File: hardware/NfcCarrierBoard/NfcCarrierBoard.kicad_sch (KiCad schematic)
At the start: 50 parts, among them J1 Barrel_Jack, J2 Conn_01x03, J3 JST SH 4, J4 Grove, J5 Conn_01x03, J6 UART, J7 Grove UART, Q1 NMOS, Q2 NMOS, SW1 RESET, U1 24AA02E-OT

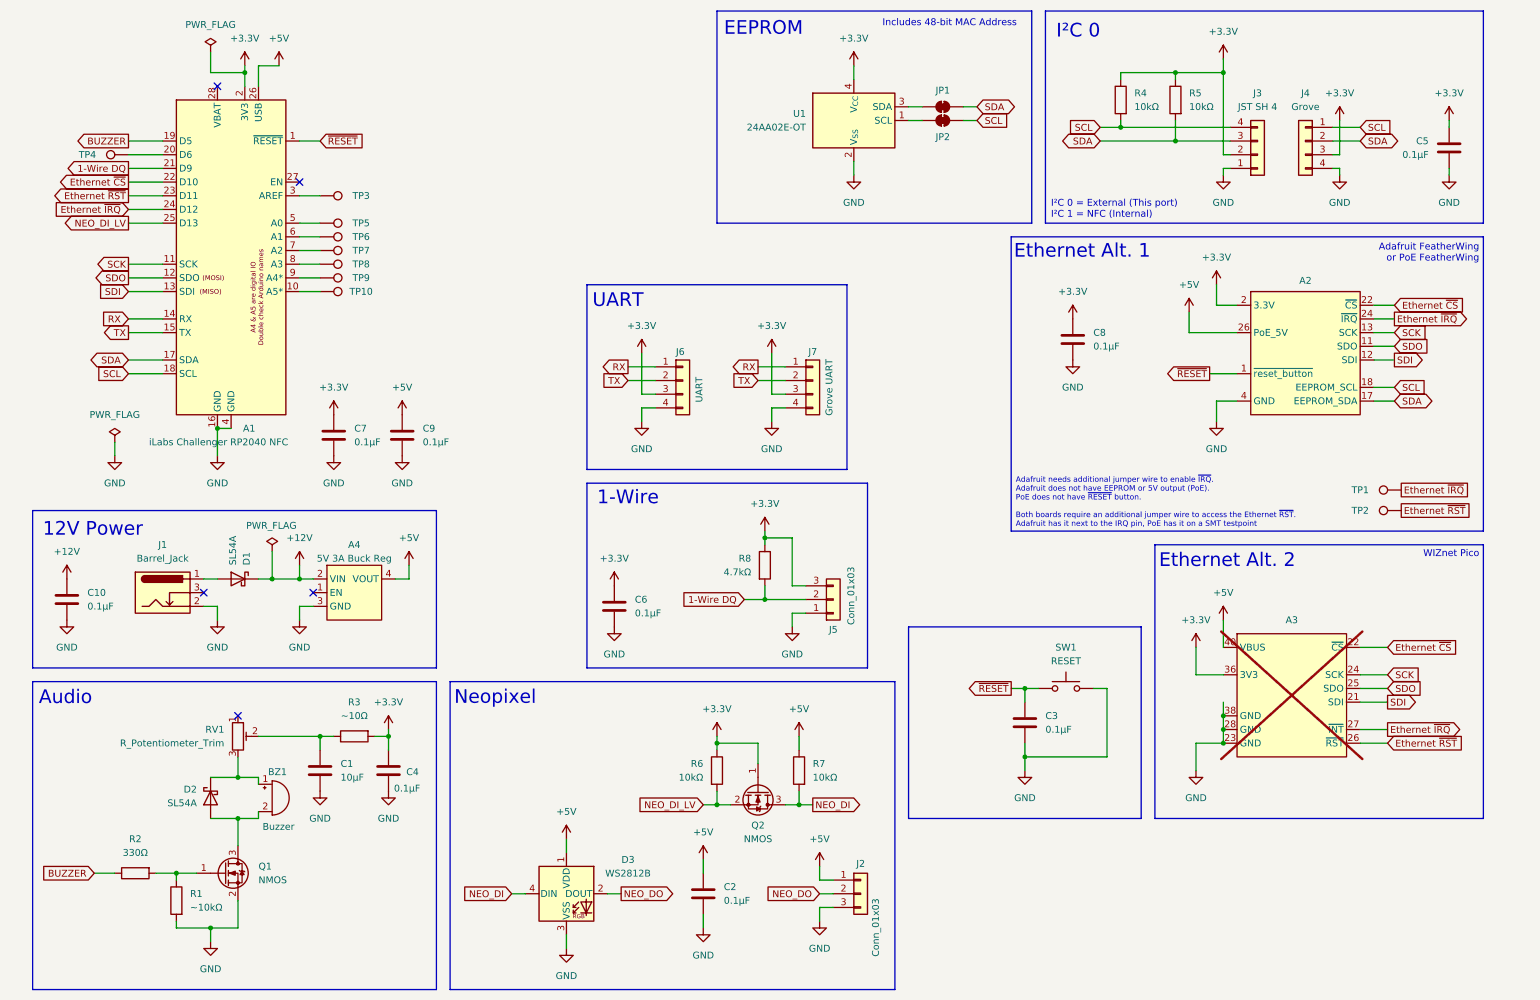
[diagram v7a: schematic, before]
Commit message: Add jumper to select between 3.3V and 5V for audio
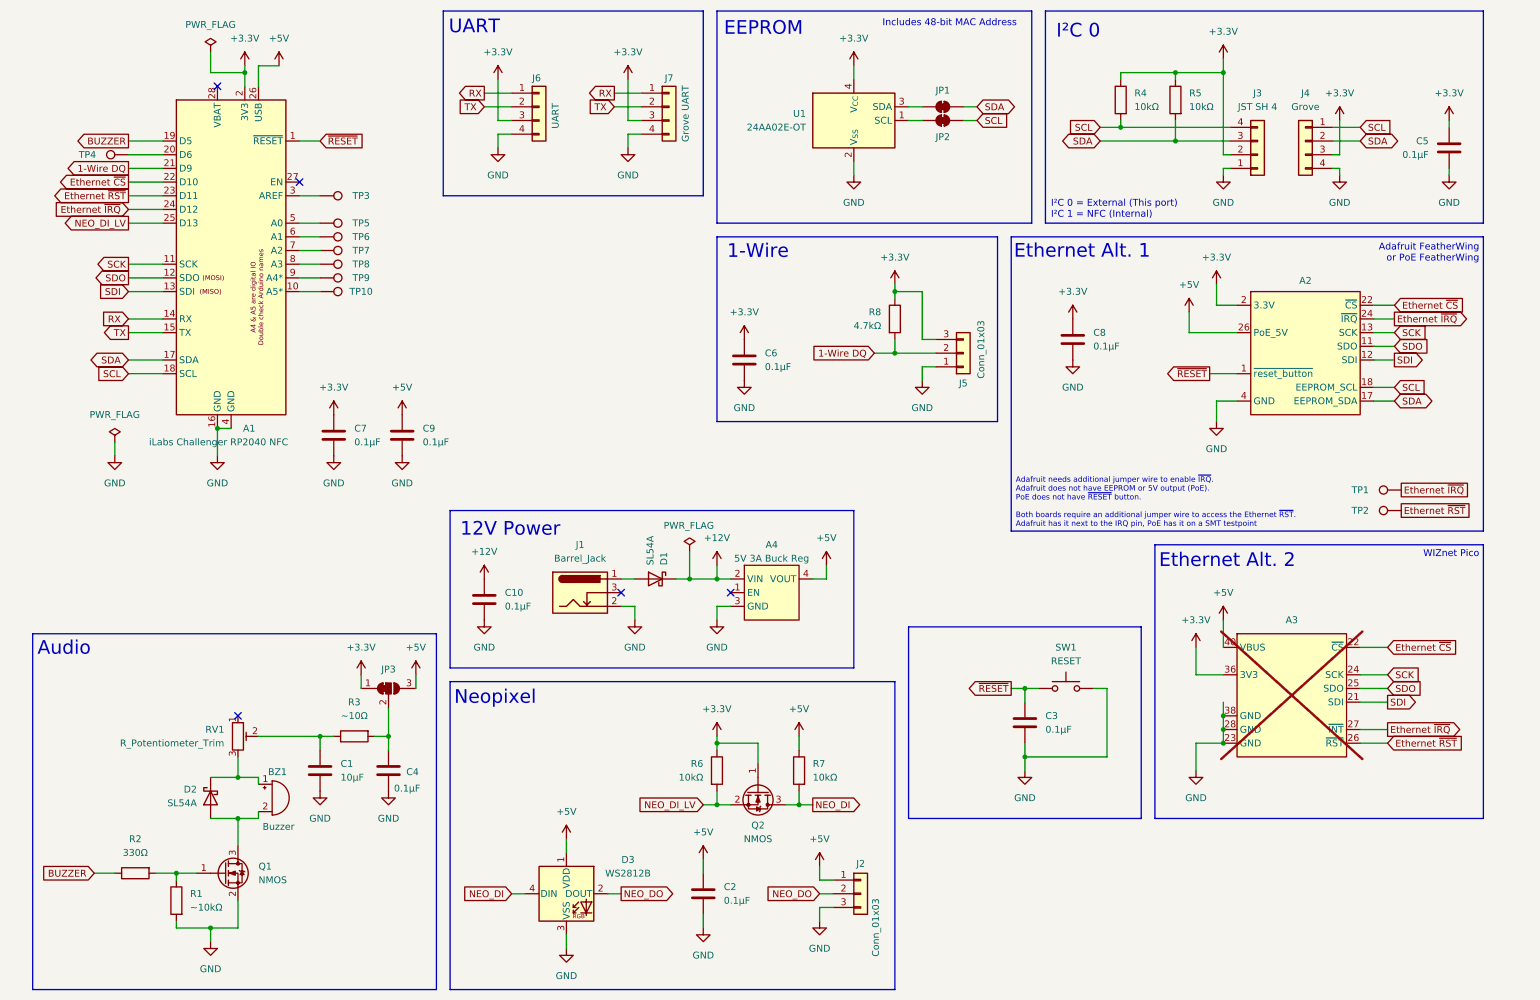
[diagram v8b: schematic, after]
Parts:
- added JP3: SolderJumper_3_Bridged12, Jumper:SolderJumper-3_P1.3mm_Bridged12_RoundedPad1.0x1.5mm, symbol Jumper:SolderJumper_3_Bridged12
- RV1: footprint Capacitor_SMD:C_0805_2012Metric_Pad1.18x1.45mm_HandSolder -> (none)
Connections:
- net +3.3V: now also JP3.1 (A); no longer C4.1, R3.2
- net +5V: now also JP3.3 (B)
- new net: C4.1, JP3.2 (C), R3.2
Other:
- moved on the sheet: A4, C10, C6, D1, J1, J5, J6, J7, R8
